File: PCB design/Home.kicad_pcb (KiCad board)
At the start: 2 copper layers, 121.9 x 157.5 mm, 18 parts, among them J1 Fan, J2 LCD, J3 EM lock, J4 ACS712 Signal, J5 Power In, J7 RFID, J8 RFID, J9 LCD, K1 SANYOU_SRD_Form_C, U1 ACS712, U3 DHT11, U5 PIR, U6 MQ2

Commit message: corrected plots
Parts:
- added R1: R, Resistor_THT:R_Axial_DIN0204_L3.6mm_D1.6mm_P5.08mm_Horizontal, F.Cu at (104.8, 71.1)
- added R2: R, Resistor_THT:R_Axial_DIN0204_L3.6mm_D1.6mm_P5.08mm_Horizontal, F.Cu at (99.7, 76.2)
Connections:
- U1 pad 2: ACS -> Net-(U1-OUT)
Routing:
- net Net-(U1-OUT): track 0.00 -> 15.0 mm
- net GND: track 433.7 -> 445.5 mm
- net ACS: track 38.3 -> 32.4 mm
- net SCK: track 96.2 -> 99.4 mm

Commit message: updated readme
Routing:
- net ACS: track 32.4 -> 33.5 mm

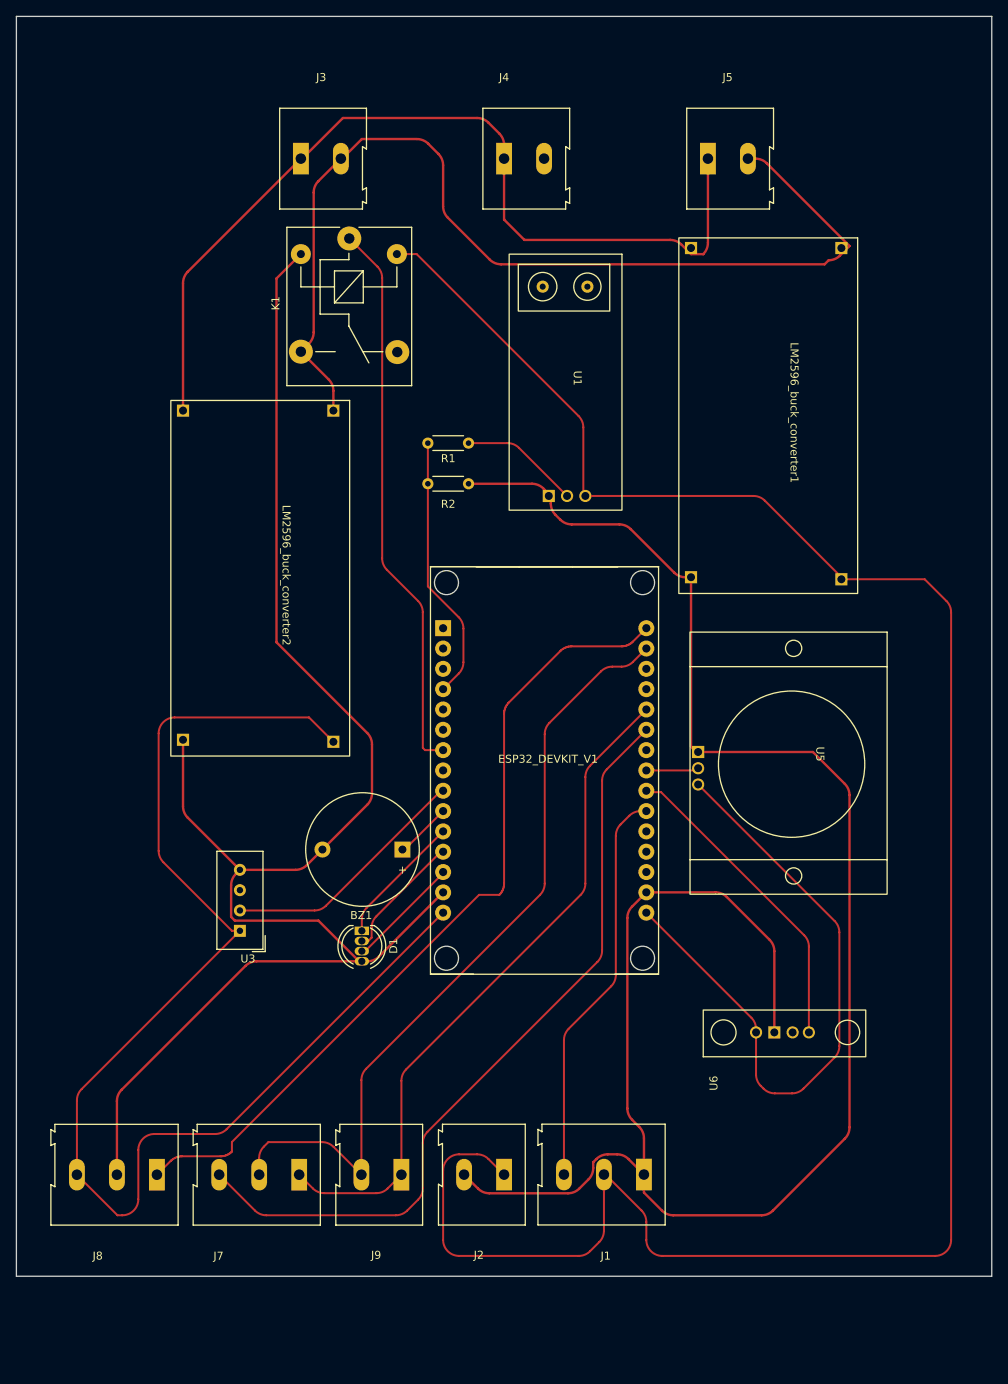
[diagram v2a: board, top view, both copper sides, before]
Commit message: PCB with thicker tracks
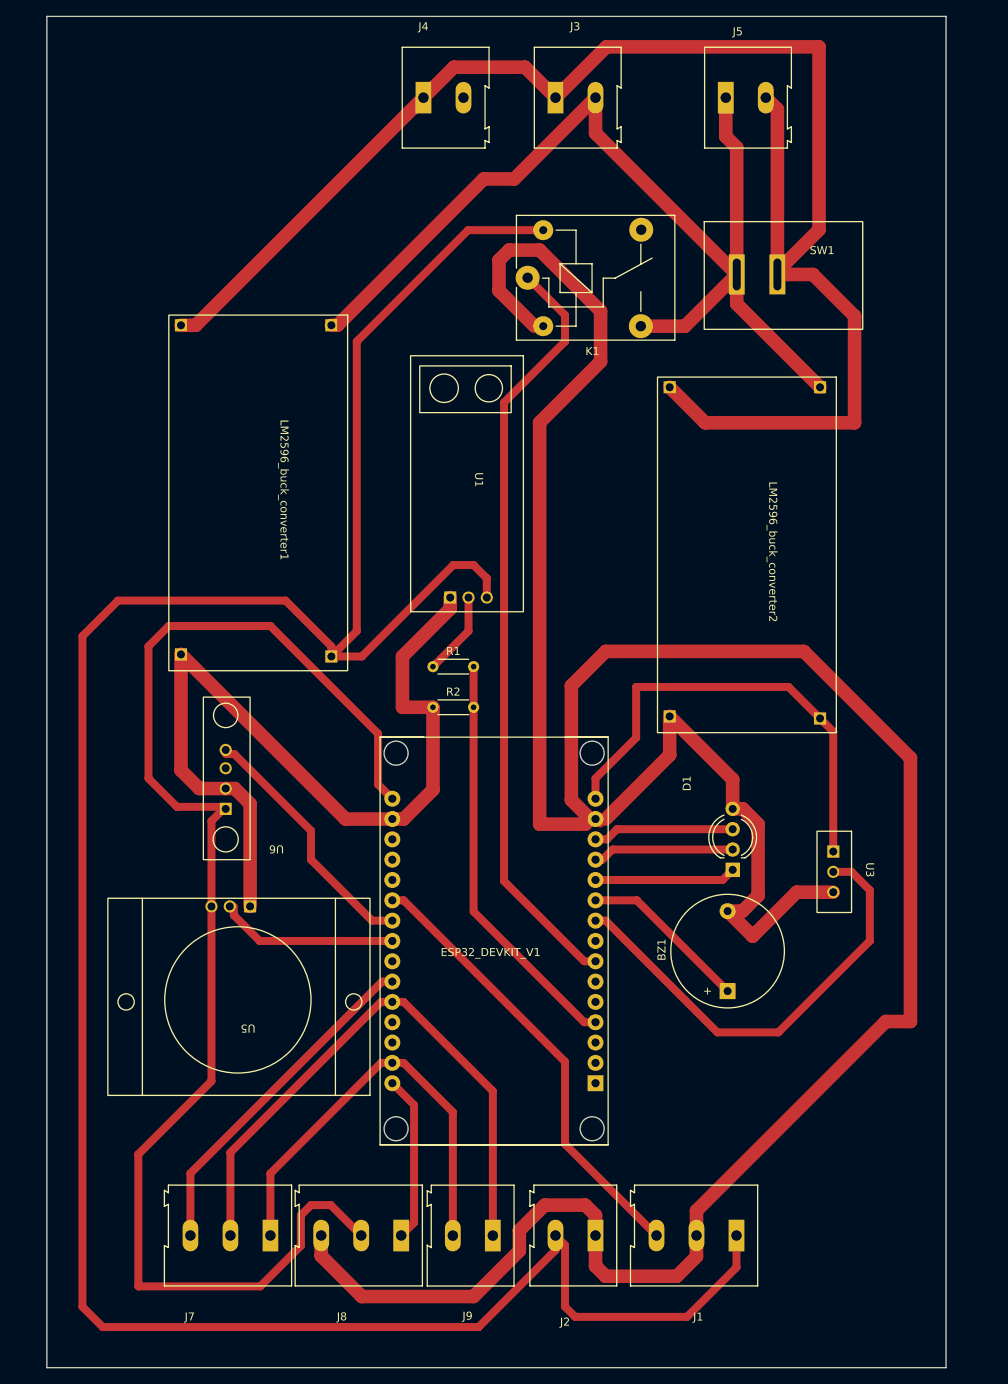
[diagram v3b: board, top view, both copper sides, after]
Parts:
- added SW1: SW_SPST, Switch_SPST:SPST - KCD1-11, F.Cu at (143.9, 48.8)
- D1: footprint LED_THT:LED_D5.0mm-4_RGB -> LED:RGB_LED
- U3: footprint Sensor:Aosong_DHT11_5.5x12.0_P2.54mm -> Sensor_temperature_humidity:DHT11_KY-015
- moved U5 85.8 mm to (72.4, 147.3), turned to 180 degrees
- moved U3 74.2 mm to (150.1, 125.2), turned to -90 degrees
- moved LM2596_buck_converter1 64.5 mm to (89.7, 55.1)
- moved U6 61.8 mm to (77.5, 123.2), turned to 180 degrees
- moved LM2596_buck_converter2 60.9 mm to (150.7, 62.9)
- moved BZ1 44.3 mm to (137.2, 139.6), turned to 90 degrees
- moved D1 41.4 mm to (130.9, 119.6), turned to 90 degrees
- moved J3 32.7 mm to (115.7, 27.9)
- moved J8 31.5 mm to (96.4, 170.2)
- moved R1 28.3 mm to (100.3, 99.1), turned to 0 degrees
- moved R2 27.9 mm to (100.3, 104.1)
- moved K1 22.8 mm to (112.2, 50.5), turned to 0 degrees
- moved ESP32_DEVKIT_V1 22.2 mm to (108.0, 133.3), turned to 180 degrees
- moved U1 17.7 mm to (111.6, 60.2)
- moved J1 13.8 mm to (138.3, 170.2)
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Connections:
- J1 pad 1: GND -> +5V
- J1 pad 2: +5V -> GND
- J2 pad 1: +5V -> GND
- J2 pad 2: GND -> +5V
- J5 pad 1: -12V -> +12V
- J5 pad 2: +12V -> -12V
- J7 pad 1: SDA -> SCK
- J7 pad 2: SCK -> SDA
- J8 pad 2: GND -> 3V3
- J8 pad 3: +3.3V -> GND
- R2 pad 1: ACS -> GND
- R2 pad 2: GND -> ACS
- U3 pad 3: unconnected-(U3-NC-Pad3) -> GND
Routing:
- net +3.3V: track 159.9 -> 58.0 mm
- net 3V3: track 80.2 -> 172.2 mm
- net -12V: track 115.5 -> 200.7 mm
- net MOSI: track 103.1 -> 20.8 mm
- net MISO: track 97.7 -> 42.9 mm
- net +5V: track 270.9 -> 320.0 mm
- net SCK: track 99.4 -> 54.3 mm
- net GND: track 445.6 -> 488.3 mm
- net RELAY: track 69.9 -> 96.1 mm
- net DHT: track 31.5 -> 56.7 mm
- net ACS: track 33.5 -> 51.6 mm
- net PIR: track 6.98 -> 22.2 mm
- net BUZZ: track 7.07 -> 21.2 mm
- net SDA: track 85.0 -> 73.7 mm
- net MQ2: track 39.4 -> 31.6 mm
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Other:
- board size 121.9 x 157.5 mm -> 112.4 x 168.9 mm

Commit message: final edits
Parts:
- removed J9: LCD, TerminalBlock:TerminalBlock_Altech_AK300-2_P5.00mm
- added C1: C, Capacitor_THT:C_Disc_D3.8mm_W2.6mm_P2.50mm, F.Cu at (120.7, 101.6)
- added J6: LCD, TerminalBlock:TerminalBlock_Altech_AK300-3_P5.00mm, F.Cu at (113.2, 170.2)
- moved J2 10.8 mm to (131.4, 171.4)
- moved J1 10.6 mm to (148.8, 171.4)
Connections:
- ESP32_DEVKIT_V1 pad 24: unconnected-(ESP32_DEVKIT_V1-GPIO18/SCK-Pad24) -> SCK
- ESP32_DEVKIT_V1 pad 28: unconnected-(ESP32_DEVKIT_V1-GPIO1/TXD0-Pad28) -> RESET
- ESP32_DEVKIT_V1 pad 29: SCK -> SCL
- J7 pad 1: SCK -> SDA
- J7 pad 2: SDA -> MISO
- J7 pad 3: MISO -> SCK
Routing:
- net GND: track 488.3 -> 398.1 mm
- net RESET: track 0.00 -> 30.2 mm
- net SCL: track 0.00 -> 24.9 mm
- net +3.3V: track 58.0 -> 70.9 mm
- net Fan: track 56.4 -> 65.6 mm
- net SCK: track 54.3 -> 48.3 mm
- net RELAY: track 96.1 -> 91.9 mm
- net -12V: track 200.7 -> 198.2 mm
- net 3V3: track 172.2 -> 173.1 mm
- net MISO: track 42.9 -> 42.2 mm
- net +12V: track 130.1 -> 129.6 mm
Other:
- board size 112.4 x 168.9 mm -> 104.8 x 168.9 mm
